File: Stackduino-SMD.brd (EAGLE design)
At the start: 62.5 x 66.7 mm, 49 parts

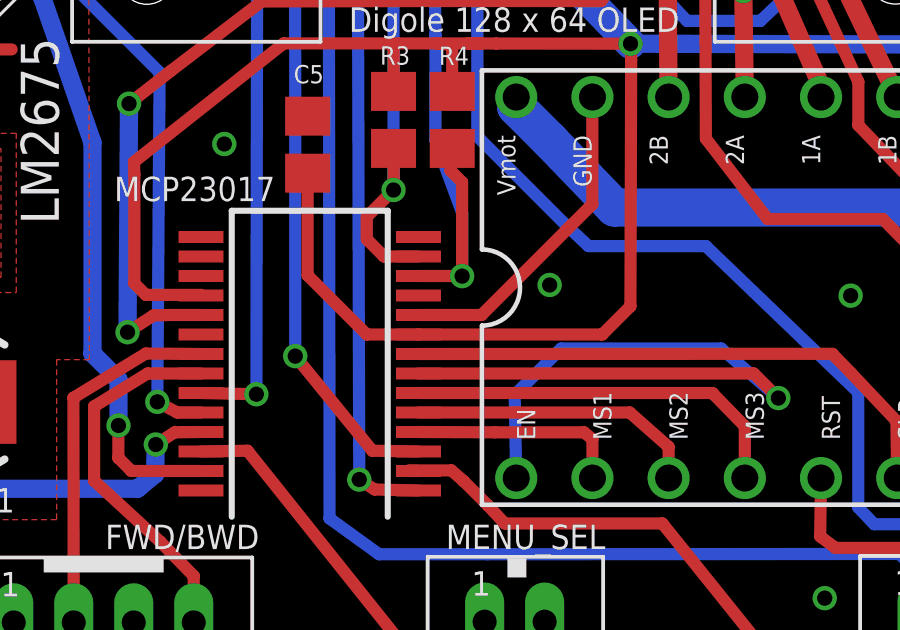
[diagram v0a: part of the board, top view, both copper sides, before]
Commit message: Amended cap values on crystal
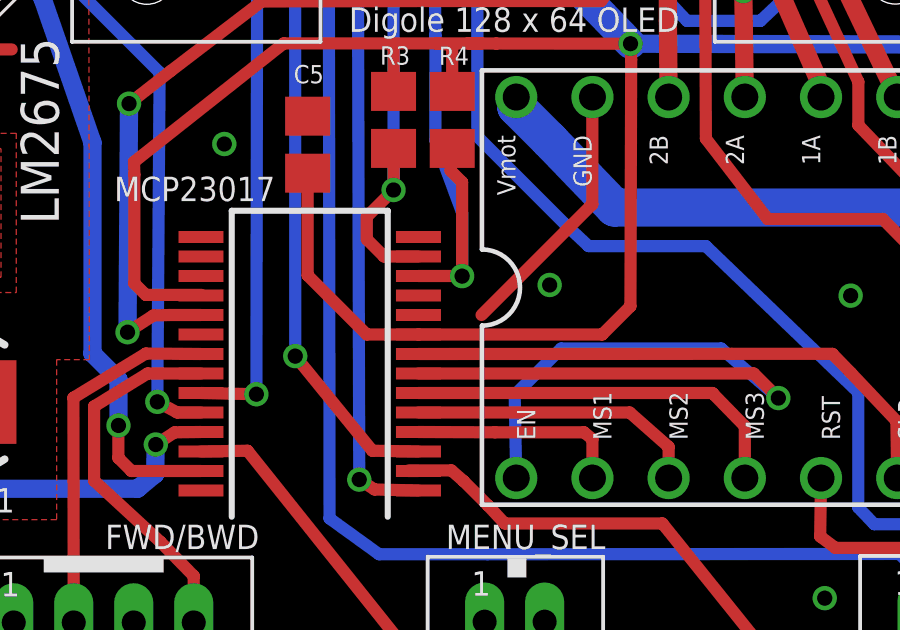
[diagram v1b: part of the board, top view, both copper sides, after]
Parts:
- C11, C12: value 0.1uF -> 22pF
- R6, R7: value 220K -> 220 Ohm
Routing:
- net GND: track 34.9 -> 32.8 mm
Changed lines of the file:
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@@
 <?xml version="1.0" encoding="utf-8"?>
 <!DOCTYPE eagle SYSTEM "eagle.dtd">
-<eagle version="6.4">
+<eagle version="6.5.0">
 <drawing>
 <settings>
@@
 <layer number="23" name="tOrigins" color="15" fill="1" visible="yes" active="yes"/>
 <layer number="24" name="bOrigins" color="15" fill="1" visible="yes" active="yes"/>
-<layer number="25" name="tNames" color="7" fill="1" visible="no" active="yes"/>
+<layer number="25" name="tNames" color="7" fill="1" visible="yes" active="yes"/>
 <layer number="26" name="bNames" color="7" fill="1" visible="no" active="yes"/>
 <layer number="27" name="tValues" color="7" fill="1" visible="no" active="yes"/>
@@
 <attribute name="VALUE" x="15.8526" y="57.0894" size="1.27" layer="27" rot="R180"/>
 </element>
-<element name="R6" library="eagle-ltspice" package="R0805" value="220K" x="47.1962" y="49.6726" smashed="yes" rot="R90">
+<element name="R6" library="eagle-ltspice" package="R0805" value="220 Ohm" x="47.1962" y="49.6726" smashed="yes" rot="R90">
 <attribute name="NAME" x="47.8634" y="47.5772" size="0.8128" layer="25" rot="R180"/>
 <attribute name="VALUE" x="49.7362" y="48.4026" size="1.27" layer="27" rot="R90"/>
@@
 <attribute name="SPICEPREFIX" value="R" x="47.1962" y="49.6726" size="1.778" layer="27" rot="R90" display="off"/>
 </element>
-<element name="R7" library="eagle-ltspice" package="R0805" value="220K" x="46.3266" y="53.1466" smashed="yes" rot="R180">
+<element name="R7" library="eagle-ltspice" package="R0805" value="220 Ohm" x="46.3266" y="53.1466" smashed="yes" rot="R180">
 <attribute name="NAME" x="47.9776" y="54.9246" size="0.8128" layer="25" rot="R180"/>
 <attribute name="VALUE" x="47.5966" y="55.6866" size="1.27" layer="27" rot="R180"/>
@@
 <attribute name="VALUE" x="44.069" y="48.3362" size="1.27" layer="27" ratio="10" rot="R90"/>
 </element>
-<element name="C12" library="eagle-ltspice" package="C0805" value="0.1uF" x="35.5346" y="56.515" smashed="yes" rot="R180">
+<element name="C12" library="eagle-ltspice" package="C0805" value="22pF" x="35.5346" y="56.515" smashed="yes" rot="R180">
 <attribute name="SPICEMODEL" value="NONE" x="35.5346" y="56.515" size="1.778" layer="27" rot="R180" display="off"/>
 <attribute name="SPICEPREFIX" value="C" x="35.5346" y="56.515" size="1.778" layer="27" rot="R180" display="off"/>
@@
 <attribute name="VALUE" x="36.8046" y="59.055" size="1.27" layer="27" rot="R180"/>
 </element>
-<element name="C11" library="eagle-ltspice" package="C0805" value="0.1uF" x="44.45" y="50.546" smashed="yes">
+<element name="C11" library="eagle-ltspice" package="C0805" value="22pF" x="44.45" y="50.546" smashed="yes">
 <attribute name="SPICEMODEL" value="NONE" x="44.45" y="50.546" size="1.778" layer="27" display="off"/>
 <attribute name="SPICEPREFIX" value="C" x="44.45" y="50.546" size="1.778" layer="27" display="off"/>
@@
 <contactref element="U$2" pad="GND@2"/>
 <contactref element="U$2" pad="GND@1"/>
-<contactref element="MCP23017" pad="10"/>
 <contactref element="ICSP" pad="6"/>
 <contactref element="DB15" pad="5"/>
@@
 <contactref element="MENU_SEL" pad="P1"/>
 <contactref element="START/STOP" pad="P1"/>
-<contactref element="FWD/BWD" pad="P3"/>
 <contactref element="FWD/BWD" pad="P1"/>
 <contactref element="ON/OFF" pad="P2"/>
 <via x="58.4708" y="61.722" extent="1-16" drill="0.508"/>
-<wire x1="27.123" y1="27.193" x2="29.225" y2="27.193" width="0.4064" layer="1"/>
 <wire x1="29.225" y1="27.193" x2="32.9184" y2="30.8864" width="0.4064" layer="1"/>
 <wire x1="32.9184" y1="30.8864" x2="32.9184" y2="34.455" width="0.4064" layer="1"/>
@@
 <contactref element="DB15" pad="10"/>
 <contactref element="FT232RL" pad="26"/>
+<contactref element="MCP23017" pad="10"/>
+<contactref element="FWD/BWD" pad="P3"/>
 </signal>
 <signal name="N$5">

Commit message: changes inc battery monitor
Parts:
- added ENCODER1: JST-PH_3-PIN_HEADER, SRG:JST_B3B-PH_HEADER
- added MENU_SEL1: JST-PH_2-PIN_HEADER, SRG:JST_B2B-PH_HEADER
- added MP2, MP3: NOT SURE YET, sym:SOT23
- added R11, R12, R14: 10K, eagle-ltspice:R0805
- added R13: 150 Ohm, eagle-ltspice:R0805
- added R15: 4.7K, eagle-ltspice:R0805
- moved MENU_SEL 2.91 mm to (33.3, 17.0)
- moved C1 1.91 mm to (2.57, 58.7)
- moved BATT 1.82 mm to (8.88, 50.6)
- moved R2 1.75 mm to (15.0, 56.3)
- moved R1 1.66 mm to (15.9, 58.0)
- moved LTC2950 1.52 mm to (9.02, 57.1)
- moved D1 1.49 mm to (2.57, 63.6)
- moved LTC4412 0.76 mm to (12.3, 61.3)
- moved R0 0.34 mm to (17.8, 62.7)
- moved 12VDC 0.25 mm to (8.24, 76.5)
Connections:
- net N$10 renamed GATE
- net VDD renamed BATTVIN
- new net BATT_FET: ATMEGA328P.26, R13.1
- new net BATT_SENSE: ATMEGA328P.25, R14.1, R15.2
- new net BATT_VOLT: MP3.3
- new net EXTRA_INPUT: MCP23017.28, MENU_SEL1.P1
- new net N$12: MP3.1, R13.2
- new net N$16: MP3.2, R14.2
- new net N$8: MCP23017.18, R12.1
- new net N$9: A4988_CARRIER.VMOT, MP2.2
- net ALOG1: now also ATMEGA328P.19; no longer ATMEGA328P.25
- net ALOG2: now also ATMEGA328P.22; no longer ATMEGA328P.26
- net ENCSWITCH: now also MENU_SEL.P1; no longer MENU_SEL.P2
- net GND: now also MENU_SEL.P2, MENU_SEL1.P2, R15.1; no longer MENU_SEL.P1
- net PBUTTON: now also R11.1
- net V+: now also MP2.3, R11.2; no longer A4988_CARRIER.VMOT
- net VCC: now also MP2.1, R12.2; no longer MCP23017.18
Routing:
- net ALOG1: track 34.4 -> 22.1 mm
- net ALOG2: track 42.4 -> 30.9 mm
- net GND: track 32.8 -> 23.6 mm, vias 11 -> 13
- net EXTRA_INPUT: track 0.00 -> 8.12 mm
- net PC1: track 46.8 -> 54.0 mm
- net BATT_FET: track 0.00 -> 5.68 mm
- net BATT_SENSE: track 0.00 -> 5.52 mm
- net N$12: track 0.00 -> 5.04 mm
- net STAT: track 70.9 -> 66.2 mm
- net VCC: track 276.2 -> 280.1 mm, vias 9 -> 10
- net N$8: track 0.00 -> 3.57 mm
- net PC0: track 52.8 -> 55.5 mm
- net DIG1: track 68.3 -> 71.0 mm
- net INT: track 43.0 -> 45.6 mm
- net PBUTTON: track 42.9 -> 45.5 mm
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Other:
- outline, holes or cut-outs redrawn

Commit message: latest progress
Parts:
- removed BATT: Battery Connector, adafruit:JST-PH-2-THM-RA
- removed ENCODER1: JST-PH_3-PIN_HEADER, SRG:JST_B3B-PH_HEADER
- added BATT_IN: JST-PH_3-PIN_HEADER, SRG:JST_B3B-PH_HEADER
- added R16: 10K, eagle-ltspice:R0805
- moved MP1 2.54 mm to (10.4, 45.8)
- moved MP3 0.94 mm to (20.3, 45.3)
- moved R2 0.25 mm to (15.0, 56.0)
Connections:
- new net N$10: BATT_IN.P1
- net BATTVIN: now also BATT_IN.P2; no longer BATT.1
- net GND: now also BATT_IN.P3, R16.1; no longer BATT.2
- net N$12: now also R16.2
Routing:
- net DIG1: track 71.0 -> 66.9 mm
- net N$12: track 5.04 -> 8.88 mm
- net BATTVIN: track 21.2 -> 25.1 mm
- net INT: track 45.6 -> 42.4 mm
- net VCC: track 280.1 -> 277.4 mm
- net PC0: track 55.5 -> 57.9 mm
- net PC1: track 54.0 -> 52.0 mm
- net V+: track 156.5 -> 155.0 mm
- net PBUTTON: track 45.5 -> 46.9 mm
- net GATE: track 18.0 -> 19.3 mm
- net N$16: track 1.94 -> 2.88 mm
- net ALOG2: track 30.9 -> 30.3 mm
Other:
- outline, holes or cut-outs redrawn

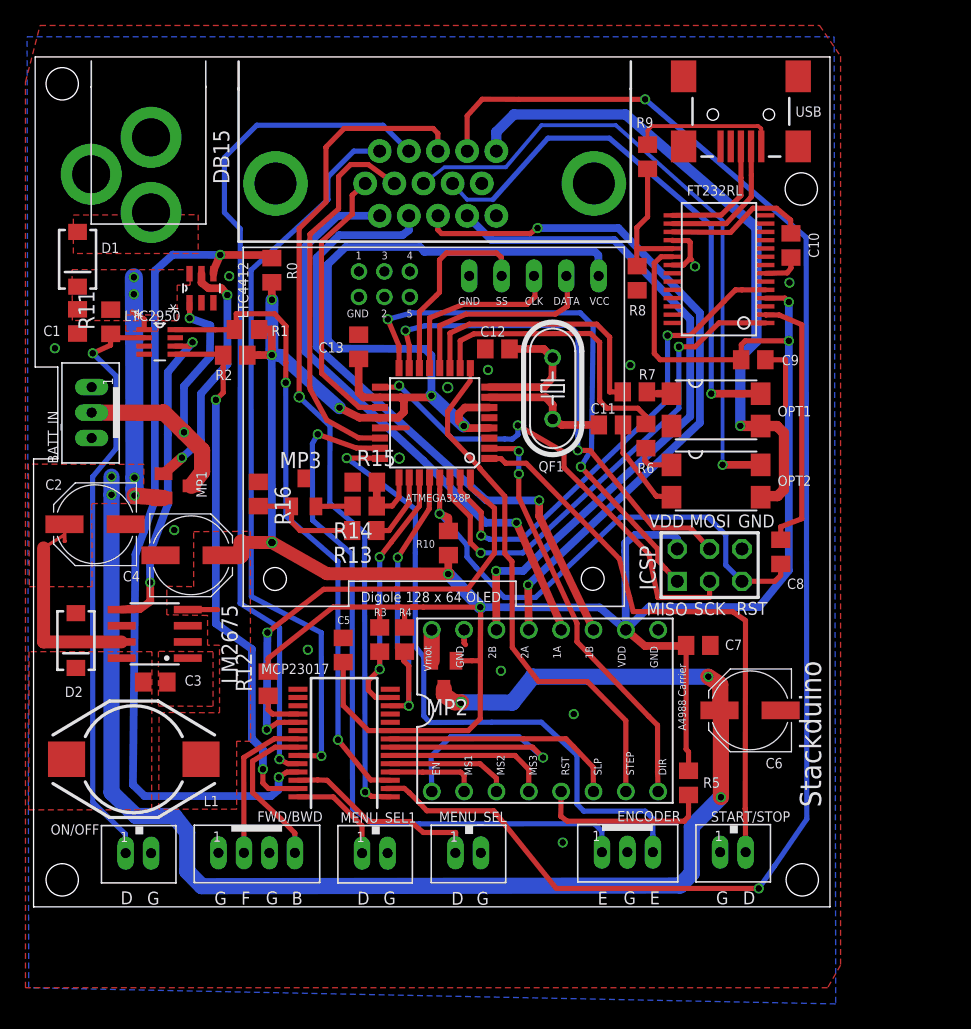
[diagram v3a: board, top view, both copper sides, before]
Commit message: Battery monitor and VMOT Mosfets added
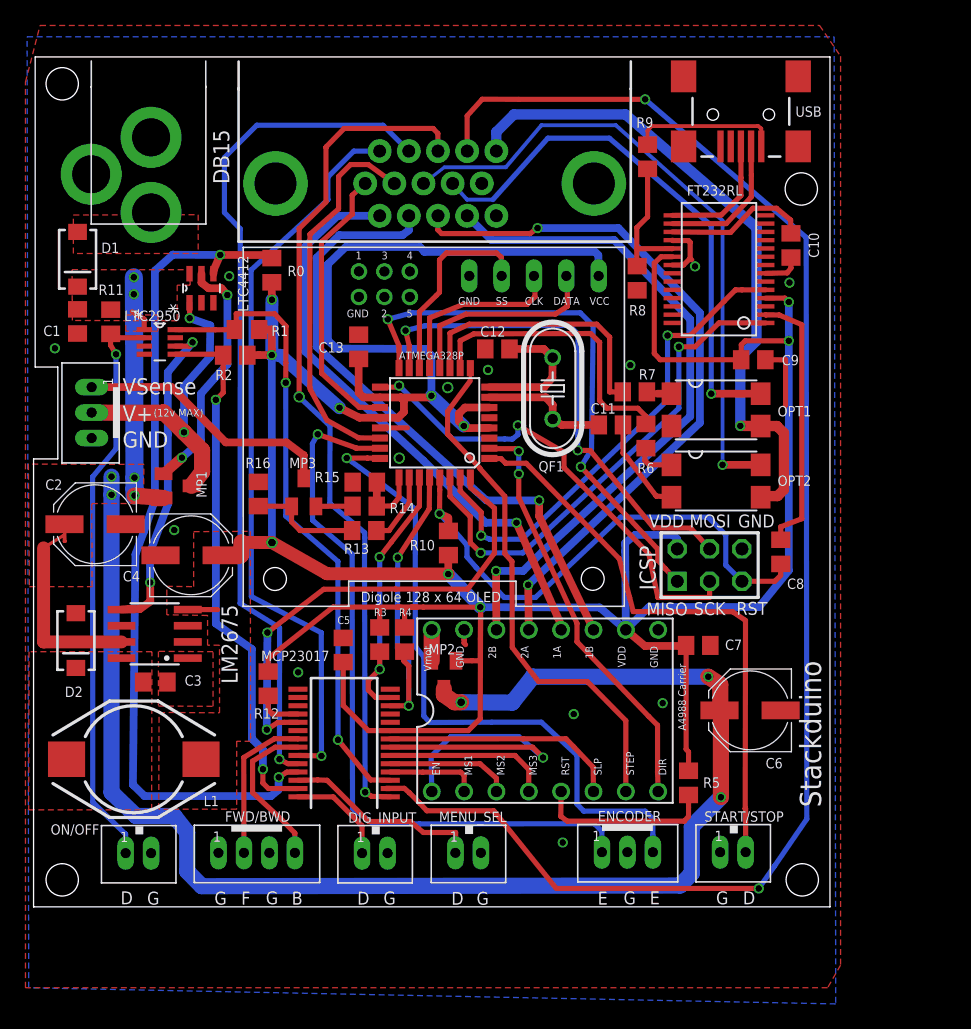
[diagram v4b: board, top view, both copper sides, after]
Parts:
- MP2, MP3: value NOT SURE YET -> NTR4501N
- renumbered MENU_SEL1 to DIG_INPUT
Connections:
- net N$28 renamed START_STOP
- net N$33 renamed FWD
- net N$35 renamed BWD
- net PC0 renamed ENC_A
- net PC1 renamed ENC_B
- removed net N$10: BATT_IN.P1
- net BATT_VOLT: now also BATT_IN.P1
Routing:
- net BATT_VOLT: track 0.00 -> 20.6 mm
- net PBUTTON: track 46.9 -> 45.4 mm
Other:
- board text added: "(12v MAX)"
- board text added: "V+"
- board text added: "VSense"

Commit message: reorganised traces to avoid inductor
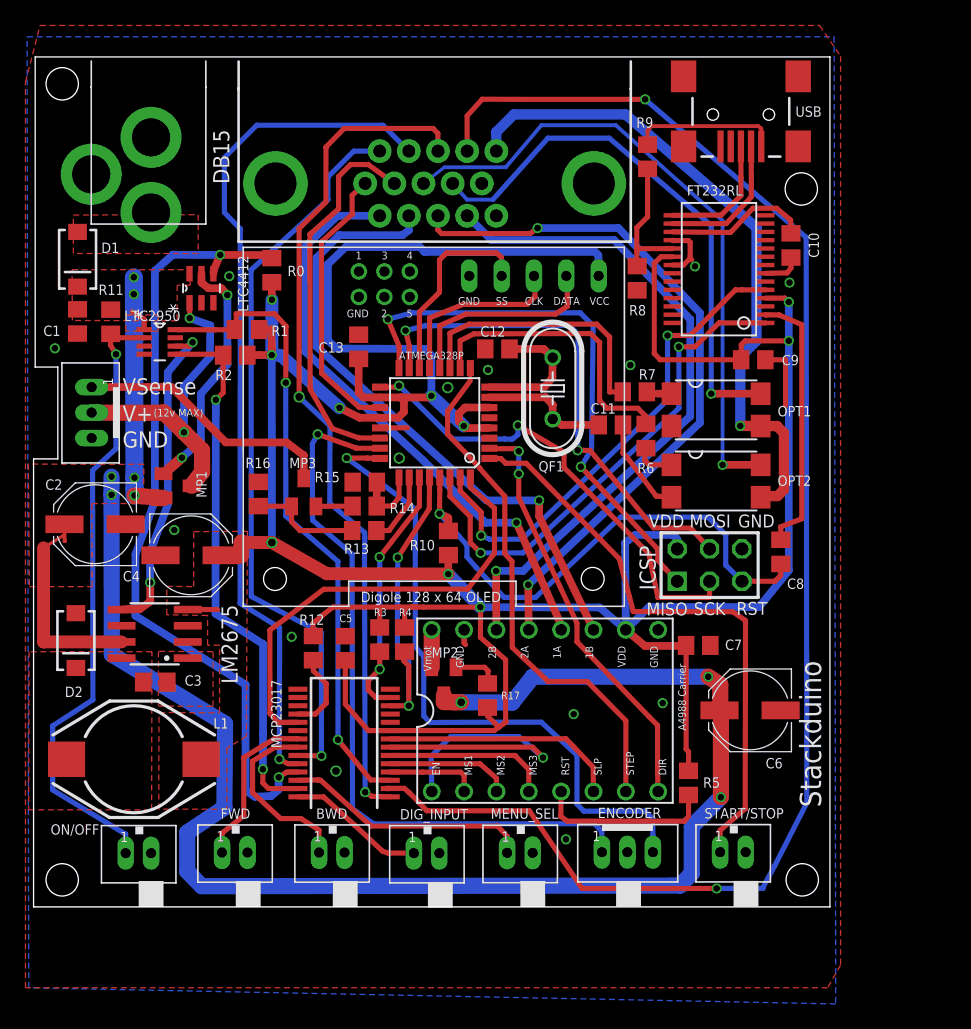
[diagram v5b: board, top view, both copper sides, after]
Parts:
- removed FWD/BWD: JST-PH_4-PIN_HEADER, SRG:JST_B4B-PH_HEADER
- added BWD, FWD: JST-PH_2-PIN_HEADER, SRG:JST_B2B-PH_HEADER
- added R17: 150 Ohm, eagle-ltspice:R0805
- moved R12 4.52 mm to (21.1, 33.0)
- moved DIG_INPUT 4.06 mm to (30.0, 17.0)
- moved MENU_SEL 4.06 mm to (37.4, 17.0)
- moved MP2 0.51 mm to (31.3, 30.4)
- moved C5 0.22 mm to (23.6, 33.0)
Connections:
- new net N$10: MP2.1, R17.1
- net BWD: now also BWD.P1; no longer FWD/BWD.P4
- net FWD: now also FWD.P1; no longer FWD/BWD.P2
- net GND: now also BWD.P2, FWD.P2, START/STOP.P2; no longer FWD/BWD.P1, FWD/BWD.P3, START/STOP.P1
- net START_STOP: now also START/STOP.P1; no longer START/STOP.P2
- net VCC: now also R17.2; no longer MP2.1
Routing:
- net VCC: track 277.4 -> 272.3 mm
- net PBUTTON: track 45.4 -> 49.4 mm
- net ENCSWITCH: track 15.7 -> 19.5 mm
- net STAT: track 66.5 -> 62.7 mm
- net N$10: track 0.00 -> 3.64 mm
- net N$8: track 3.57 -> 6.37 mm
- net EXTRA_INPUT: track 8.12 -> 10.8 mm
- net V+: track 155.0 -> 157.2 mm
- net BWD: track 12.5 -> 14.4 mm
- net N$17: track 37.5 -> 36.0 mm, vias 2 -> 0
- net START_STOP: track 45.1 -> 46.0 mm
- net FWD: track 12.2 -> 13.0 mm
- net N$9: track 2.43 -> 2.94 mm
- net GND: vias 13 -> 14
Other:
- board text removed: "B"
- board text removed: "D"
- board text removed: "E"
- board text removed: "F"
- board text removed: "G"

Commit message: Changed inductor placement
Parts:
- moved ON/OFF 4.02 mm to (10.7, 14.7)
- moved FWD 3.42 mm to (17.5, 14.7)
- moved L1 3.07 mm to (4.19, 23.0), turned to 270 degrees
- moved BWD 2.90 mm to (24.4, 14.7)
- moved DIG_INPUT 2.57 mm to (31.3, 14.7)
- moved MENU_SEL 2.46 mm to (38.2, 14.7)
- moved ENCODER 2.40 mm to (46.1, 14.7)
- moved START/STOP 2.35 mm to (54.1, 14.7)
- moved R13 1.02 mm to (24.1, 42.3)
- moved BATT_IN 0.11 mm to (3.61, 51.5)
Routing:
- net V+: track 157.2 -> 145.1 mm
- net FWD: track 13.0 -> 16.5 mm
- net BWD: track 14.4 -> 17.9 mm
- net PBUTTON: track 49.4 -> 52.7 mm
- net ENC_B: track 52.0 -> 55.3 mm, vias 1 -> 2
- net ENC_A: track 57.9 -> 61.1 mm, vias 1 -> 2
- net EXTRA_INPUT: track 10.8 -> 13.9 mm
- net ENCSWITCH: track 19.5 -> 22.2 mm
- net START_STOP: track 46.0 -> 48.3 mm
- net DIG2: track 119.9 -> 121.7 mm
- net N$2: track 14.0 -> 12.4 mm
- net N$12: track 8.88 -> 7.87 mm
- net BATT_FET: track 5.68 -> 6.60 mm
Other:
- board size 62.5 x 66.7 mm -> 62.5 x 68 mm
